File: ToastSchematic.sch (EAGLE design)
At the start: 86 parts, among them Q1 DMN63D8LDW, Q2 DMN63D8LDW, Q3 DMN63D8LDW, Q4 DMN63D8LDW, T1 BPX81, T2 BPX81, T3 BPX81, T4 BPX81, T5 BPX81, T6 BPX81, U3 DRV8839_DSS_12, U4 DRV8839_DSS_12

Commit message: finished wiring everything
still need to add toast and butter pics on the back and smash and label
stuff
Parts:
- added LED8, LED9: (no value), led:LEDCHIPLED_0603
- added R2, R3: (no value), resistor:R-US_R0603
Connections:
- new net LED1: R3.1, U$1.PC10
- new net LED2: R2.1, U$1.PC11
- new net N$22: LED8.A, R3.2
- new net N$25: LED9.A, R2.2
- net DGND: now also LED8.C, LED9.C
- net DISP_CE: now also U$1.PC12
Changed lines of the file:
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@@
 <?xml version="1.0" encoding="utf-8"?>
 <!DOCTYPE eagle SYSTEM "eagle.dtd">
-<eagle version="8.3.1">
+<eagle version="8.4.1">
 <drawing>
 <settings>
@@
 <part name="SUPPLY46" library="SparkFun-PowerSymbols" deviceset="V_BATT" device=""/>
 <part name="SUPPLY47" library="supply2" library_urn="urn:adsk.eagle:library:372" deviceset="GND" device=""/>
+<part name="R2" library="resistor" library_urn="urn:adsk.eagle:library:348" deviceset="R-US_" device="R0603" package3d_urn="urn:adsk.eagle:package:26057/1"/>
+<part name="R3" library="resistor" library_urn="urn:adsk.eagle:library:348" deviceset="R-US_" device="R0603" package3d_urn="urn:adsk.eagle:package:26057/1"/>
+<part name="LED8" library="led" library_urn="urn:adsk.eagle:library:259" deviceset="LED" device="CHIPLED_0603" package3d_urn="urn:adsk.eagle:package:15822/1"/>
+<part name="LED9" library="led" library_urn="urn:adsk.eagle:library:259" deviceset="LED" device="CHIPLED_0603" package3d_urn="urn:adsk.eagle:package:15822/1"/>
+<part name="SUPPLY48" library="supply2" library_urn="urn:adsk.eagle:library:372" deviceset="DGND" device=""/>
 </parts>
 <sheets>
@@
 <instance part="SUPPLY46" gate="G$1" x="63.5" y="142.24"/>
 <instance part="SUPPLY47" gate="GND" x="88.9" y="129.54"/>
+<instance part="R2" gate="G$1" x="213.36" y="152.4"/>
+<instance part="R3" gate="G$1" x="213.36" y="160.02"/>
+<instance part="LED8" gate="G$1" x="223.52" y="160.02" rot="R90"/>
+<instance part="LED9" gate="G$1" x="223.52" y="152.4" rot="R90"/>
+<instance part="SUPPLY48" gate="G$1" x="233.68" y="160.02" rot="R90"/>
 </instances>
 <busses>
@@
 <pinref part="U$5" gate="G$1" pin="2"/>
 <wire x1="33.02" y1="137.16" x2="35.56" y2="137.16" width="0.1524" layer="91"/>
+</segment>
+<segment>
+<pinref part="LED8" gate="G$1" pin="C"/>
+<wire x1="228.6" y1="160.02" x2="231.14" y2="160.02" width="0.1524" layer="91"/>
+<pinref part="SUPPLY48" gate="G$1" pin="DGND"/>
+<pinref part="LED9" gate="G$1" pin="C"/>
+<wire x1="228.6" y1="152.4" x2="233.68" y2="152.4" width="0.1524" layer="91"/>
+<wire x1="233.68" y1="152.4" x2="233.68" y2="160.02" width="0.1524" layer="91"/>
+<wire x1="233.68" y1="160.02" x2="231.14" y2="160.02" width="0.1524" layer="91"/>
+<junction x="231.14" y="160.02"/>
 </segment>
 </net>
@@
 </segment>
 </net>
+<net name="DISP_CE" class="0">
+<segment>
+<pinref part="U$1" gate="G$1" pin="PC12"/>
+<wire x1="127" y1="114.3" x2="137.16" y2="114.3" width="0.1524" layer="91"/>
+<label x="137.16" y="114.3" size="1.778" layer="95" xref="yes"/>
+</segment>
+</net>
+<net name="N$22" class="0">
+<segment>
+<pinref part="R3" gate="G$1" pin="2"/>
+<pinref part="LED8" gate="G$1" pin="A"/>
+<wire x1="218.44" y1="160.02" x2="220.98" y2="160.02" width="0.1524" layer="91"/>
+</segment>
+</net>
+<net name="LED1" class="0">
+<segment>
+<pinref part="U$1" gate="G$1" pin="PC10"/>
+<wire x1="127" y1="119.38" x2="132.08" y2="119.38" width="0.1524" layer="91"/>
+<label x="132.08" y="119.38" size="1.778" layer="95" xref="yes"/>
+</segment>
+<segment>
+<pinref part="R3" gate="G$1" pin="1"/>
+<wire x1="208.28" y1="160.02" x2="205.74" y2="160.02" width="0.1524" layer="91"/>
+<label x="205.74" y="160.02" size="1.778" layer="95" rot="R180" xref="yes"/>
+</segment>
+</net>
+<net name="LED2" class="0">
+<segment>
+<pinref part="U$1" gate="G$1" pin="PC11"/>
+<wire x1="127" y1="116.84" x2="142.24" y2="116.84" width="0.1524" layer="91"/>
+<label x="142.24" y="116.84" size="1.778" layer="95" xref="yes"/>
+</segment>
+<segment>
+<pinref part="R2" gate="G$1" pin="1"/>
+<wire x1="208.28" y1="152.4" x2="205.74" y2="152.4" width="0.1524" layer="91"/>
+<label x="205.74" y="152.4" size="1.778" layer="95" rot="R180" xref="yes"/>
+</segment>
+</net>
+<net name="N$25" class="0">
+<segment>
+<pinref part="R2" gate="G$1" pin="2"/>
+<pinref part="LED9" gate="G$1" pin="A"/>
+<wire x1="218.44" y1="152.4" x2="220.98" y2="152.4" width="0.1524" layer="91"/>
+</segment>
+</net>

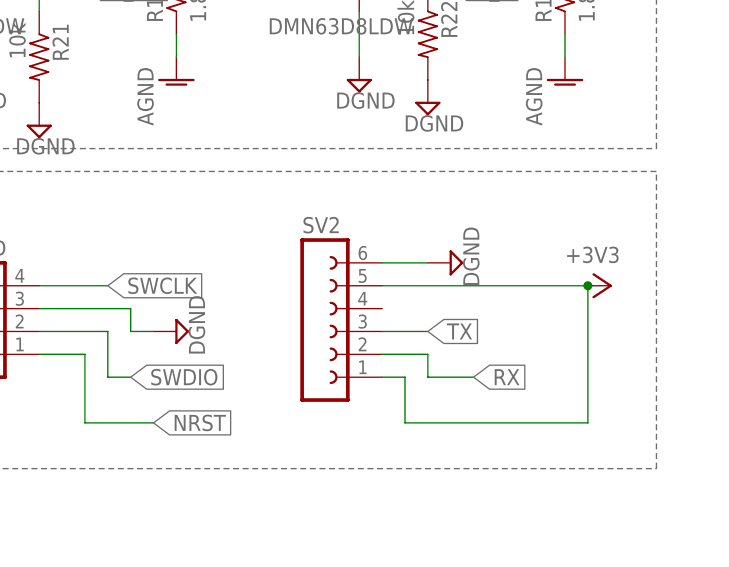
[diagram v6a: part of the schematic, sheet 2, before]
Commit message: Added art to board
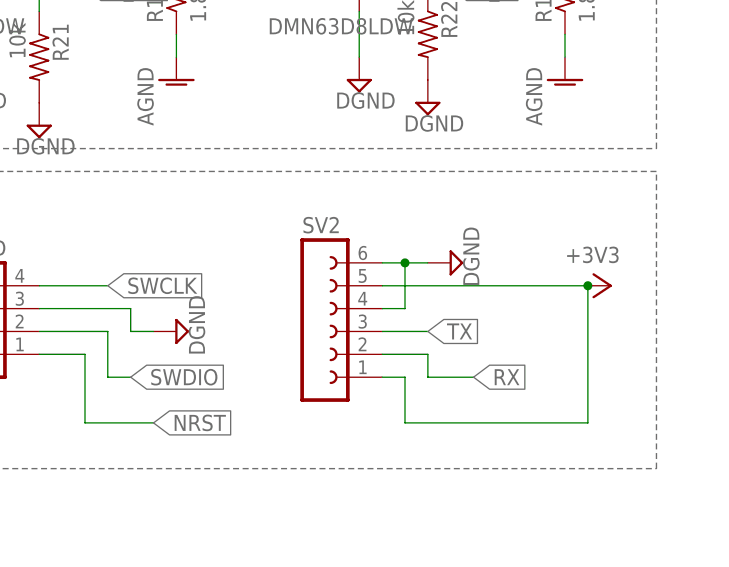
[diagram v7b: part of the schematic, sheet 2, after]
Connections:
- net DGND: now also SV2.4
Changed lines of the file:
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@@
 <segment>
 <pinref part="SUPPLY34" gate="G$1" pin="DGND"/>
-<wire x1="223.52" y1="48.26" x2="228.6" y2="48.26" width="0.1524" layer="91"/>
+<wire x1="223.52" y1="48.26" x2="226.06" y2="48.26" width="0.1524" layer="91"/>
 <pinref part="SV2" gate="G$1" pin="6"/>
+<pinref part="SV2" gate="G$1" pin="4"/>
+<wire x1="226.06" y1="48.26" x2="228.6" y2="48.26" width="0.1524" layer="91"/>
+<wire x1="223.52" y1="43.18" x2="226.06" y2="43.18" width="0.1524" layer="91"/>
+<wire x1="226.06" y1="43.18" x2="226.06" y2="48.26" width="0.1524" layer="91"/>
+<junction x="226.06" y="48.26"/>
 </segment>
 <segment>
